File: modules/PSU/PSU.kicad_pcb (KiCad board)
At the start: 2 copper layers, 28 x 16 mm, 8 parts, among them J1 Conn_01x01_Pin, J2 Conn_01x02_Pin, Q10 MMBT3904

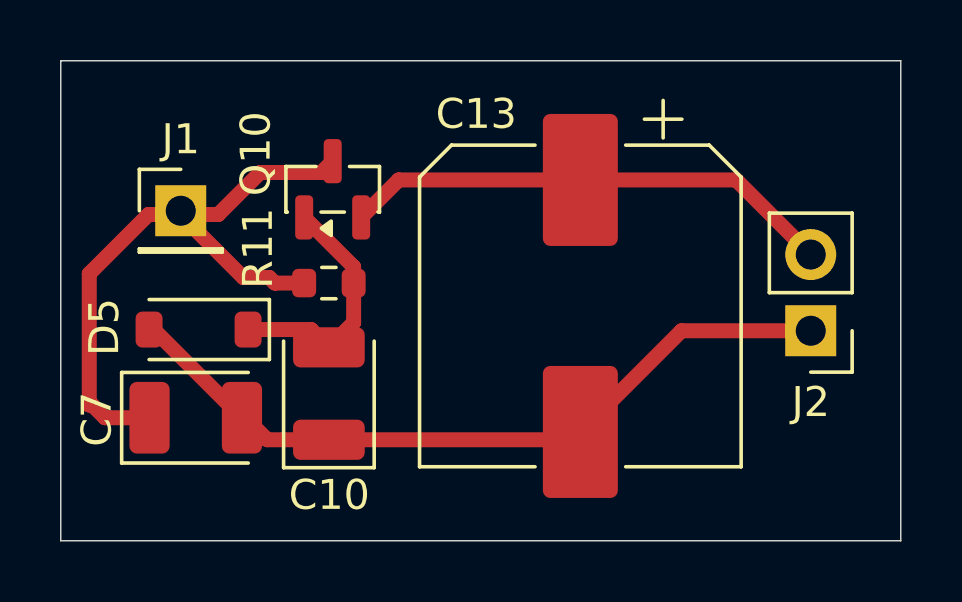
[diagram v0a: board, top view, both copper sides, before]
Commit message: PSU: added power led
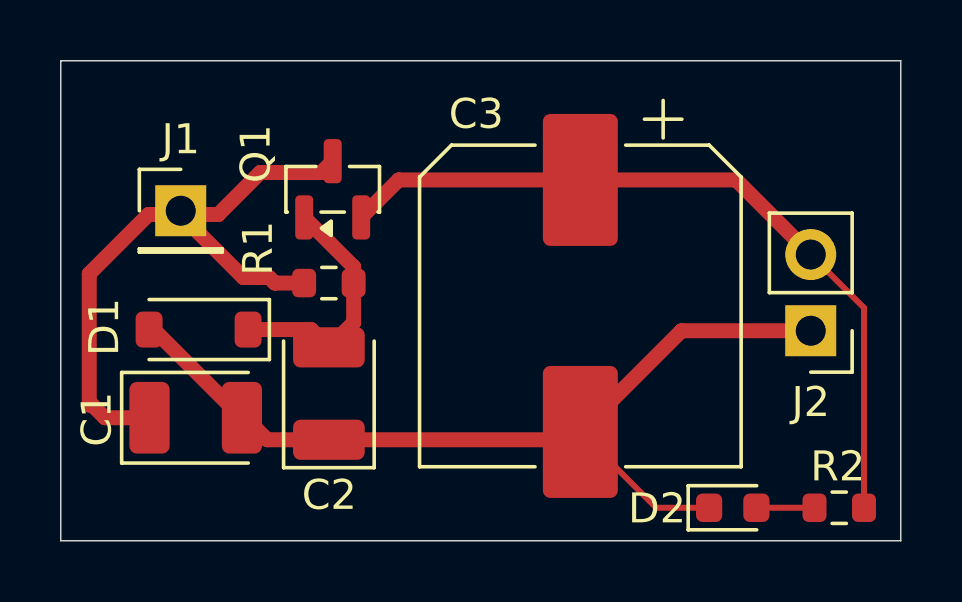
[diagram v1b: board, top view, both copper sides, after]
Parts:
- added D2: LED, LED_SMD:LED_0603_1608Metric, F.Cu at (152.4, 120.9)
- added R2: R, Resistor_SMD:R_0603_1608Metric, F.Cu at (155.9, 120.9)
- renumbered C7 to C1, C10 to C2, C13 to C3, D5 to D1, Q10 to Q1, R11 to R1
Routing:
- net VDD: track 16.5 -> 25.7 mm
- net GND: track 25.1 -> 30.4 mm
- net Net-(D2-A): track 0.00 -> 1.94 mm
